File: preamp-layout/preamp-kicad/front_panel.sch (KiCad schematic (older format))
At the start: 0 parts

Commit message: general layout work
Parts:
- added SW? (x6): SW_Push_Open, symbol Switch:SW_Push_Open
- added U?: 4021, symbol 4xxx:4021
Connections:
- net CLK: now also U?.10 (CP)
- net MISO: now also U?.3 (Q7)
- net MOSI: now also U?.11 (DS)
- new net 5V: SW?.1 (A), SW?.1 (A), SW?.1 (A), SW?.1 (A), SW?.1 (A), SW?.1 (A), U?.16 (VDD)
- new net CS: U?.9 (PL)
- new net GNDD: U?.8 (VSS)
- new net SW_CH1: SW?.2 (B), U?.7 (D0)
- new net SW_CH2: SW?.2 (B), U?.6 (D1)
- new net SW_CH3: SW?.2 (B), U?.5 (D2)
- new net SW_CH4: SW?.2 (B), U?.4 (D3)
- new net SW_CH5: SW?.2 (B), U?.13 (D4)
- new net SW_MUTE: SW?.2 (B), U?.14 (D5)
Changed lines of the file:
@@
 $Descr A4 11693 8268
 encoding utf-8
-Sheet 6 11
+Sheet 13 13
 Title ""
 Date ""
@@
 Comment4 ""
 $EndDescr
-Text HLabel 3950 3500 0    50   Output ~ 0
+$Comp
+L Switch:SW_Push_Open SW?
+U 1 1 639B5052
+P 5150 2450
+F 0 "SW?" V 5104 2527 50  0000 L CNN
+F 1 "SW_Push_Open" V 5195 2527 50  0000 L CNN
+F 2 "" H 5150 2650 50  0001 C CNN
+F 3 "~" H 5150 2650 50  0001 C CNN
+	1    5150 2450
+	0    1    1    0
+$EndComp
+Text GLabel 5150 2250 1    50   UnSpc ~ 0
+5V
+$Comp
+L Switch:SW_Push_Open SW?
+U 1 1 639B5BA4
+P 5950 2450
+F 0 "SW?" V 5904 2527 50  0000 L CNN
+F 1 "SW_Push_Open" V 5995 2527 50  0000 L CNN
+F 2 "" H 5950 2650 50  0001 C CNN
+F 3 "~" H 5950 2650 50  0001 C CNN
+	1    5950 2450
+	0    1    1    0
+$EndComp
+Text GLabel 5950 2250 1    50   UnSpc ~ 0
+5V
+$Comp
+L Switch:SW_Push_Open SW?
+U 1 1 639B6392
+P 6750 2450
+F 0 "SW?" V 6704 2527 50  0000 L CNN
+F 1 "SW_Push_Open" V 6795 2527 50  0000 L CNN
+F 2 "" H 6750 2650 50  0001 C CNN
+F 3 "~" H 6750 2650 50  0001 C CNN
+	1    6750 2450
+	0    1    1    0
+$EndComp
+Text GLabel 6750 2250 1    50   UnSpc ~ 0
+5V
+$Comp
+L Switch:SW_Push_Open SW?
+U 1 1 639B63A7
+P 7550 2450
+F 0 "SW?" V 7504 2527 50  0000 L CNN
+F 1 "SW_Push_Open" V 7595 2527 50  0000 L CNN
+F 2 "" H 7550 2650 50  0001 C CNN
+F 3 "~" H 7550 2650 50  0001 C CNN
+	1    7550 2450
+	0    1    1    0
+$EndComp
+Text GLabel 7550 2250 1    50   UnSpc ~ 0
+5V
+$Comp
+L Switch:SW_Push_Open SW?
+U 1 1 639B8372
+P 8350 2450
+F 0 "SW?" V 8304 2527 50  0000 L CNN
+F 1 "SW_Push_Open" V 8395 2527 50  0000 L CNN
+F 2 "" H 8350 2650 50  0001 C CNN
+F 3 "~" H 8350 2650 50  0001 C CNN
+	1    8350 2450
+	0    1    1    0
+$EndComp
+Text GLabel 8350 2250 1    50   UnSpc ~ 0
+5V
+$Comp
+L Switch:SW_Push_Open SW?
+U 1 1 639B8387
+P 9150 2450
+F 0 "SW?" V 9104 2527 50  0000 L CNN
+F 1 "SW_Push_Open" V 9195 2527 50  0000 L CNN
+F 2 "" H 9150 2650 50  0001 C CNN
+F 3 "~" H 9150 2650 50  0001 C CNN
+	1    9150 2450
+	0    1    1    0
+$EndComp
+Text GLabel 9150 2250 1    50   UnSpc ~ 0
+5V
+$Comp
+L 4xxx:4021 U?
+U 1 1 639BBE1A
+P 10100 4550
+F 0 "U?" H 10100 5531 50  0000 C CNN
+F 1 "4021" H 10100 5440 50  0000 C CNN
+F 2 "" H 10100 4700 50  0001 C CNN
+F 3 "https://assets.nexperia.com/documents/data-sheet/HEF4021B.pdf" H 10100 4700 50  0001 C CNN
+	1    10100 4550
+	1    0    0    -1
+$EndComp
+Text GLabel 10100 3450 1    50   UnSpc ~ 0
+5V
+Wire Wire Line
+	10100 3750 10100 3450
+Text Label 9550 4450 2    50   ~ 0
+SW_CH1
+Text Label 9550 4550 2    50   ~ 0
+SW_CH2
+Text Label 9550 4650 2    50   ~ 0
+SW_CH3
+Text Label 9550 4750 2    50   ~ 0
+SW_CH4
+Text Label 9550 4850 2    50   ~ 0
+SW_CH5
+Text Label 9550 4950 2    50   ~ 0
+SW_MUTE
+Wire Wire Line
+	9700 4450 9550 4450
+Wire Wire Line
+	9550 4650 9700 4650
+Wire Wire Line
+	9550 4550 9700 4550
+Wire Wire Line
+	9700 4750 9550 4750
+Wire Wire Line
+	9700 4850 9550 4850
+Wire Wire Line
+	9700 4950 9550 4950
+$Comp
+L power:GNDD #PWR?
+U 1 1 639C488C
+P 10100 5350
+F 0 "#PWR?" H 10100 5100 50  0001 C CNN
+F 1 "GNDD" H 10104 5195 50  0000 C CNN
+F 2 "" H 10100 5350 50  0001 C CNN
+F 3 "" H 10100 5350 50  0001 C CNN
+	1    10100 5350
+	1    0    0    -1
+$EndComp
+Text HLabel 10650 4150 2    50   Output ~ 0
 MISO
-Text HLabel 3950 3700 0    50   Input ~ 0
+Text HLabel 9550 4250 0    50   Input ~ 0
 MOSI
-Text HLabel 3950 3900 0    50   Input ~ 0
+Text HLabel 9550 3950 0    50   Input ~ 0
 CLK
-Text HLabel 3950 4100 0    50   Input ~ 0
-CS_VOL_LIGHT
-Text HLabel 3950 4300 0    50   Input ~ 0
-CS_SELECT_LIGHT
-Text HLabel 3950 4500 0    50   Input ~ 0
-CS_VOL_ENCODER
-Text HLabel 3950 4700 0    50   Input ~ 0
-CS_SELECT_ENCODER
+Text HLabel 9550 4150 0    50   Input ~ 0
+CS
+Wire Wire Line
+	9550 4250 9700 4250
+Wire Wire Line
+	9550 4150 9700 4150
+Wire Wire Line
+	9550 3950 9700 3950
+Wire Wire Line
+	10500 4150 10650 4150
+Text Label 5150 2650 3    50   ~ 0
+SW_CH1
+Text Label 5950 2650 3    50   ~ 0
+SW_CH2
+Text Label 6750 2650 3    50   ~ 0
+SW_CH3
+Text Label 7550 2650 3    50   ~ 0
+SW_CH4
+Text Label 8350 2650 3    50   ~ 0
+SW_CH5
+Text Label 9150 2650 3    50   ~ 0
+SW_MUTE
+Text HLabel 6900 4000 2    50   UnSpc ~ 0
+tone_ctl_1
+Text HLabel 6900 4150 2    50   UnSpc ~ 0
+tone_ctl_2
+Text HLabel 6900 4300 2    50   UnSpc ~ 0
+tone_ctl_3
 $EndSCHEMATC

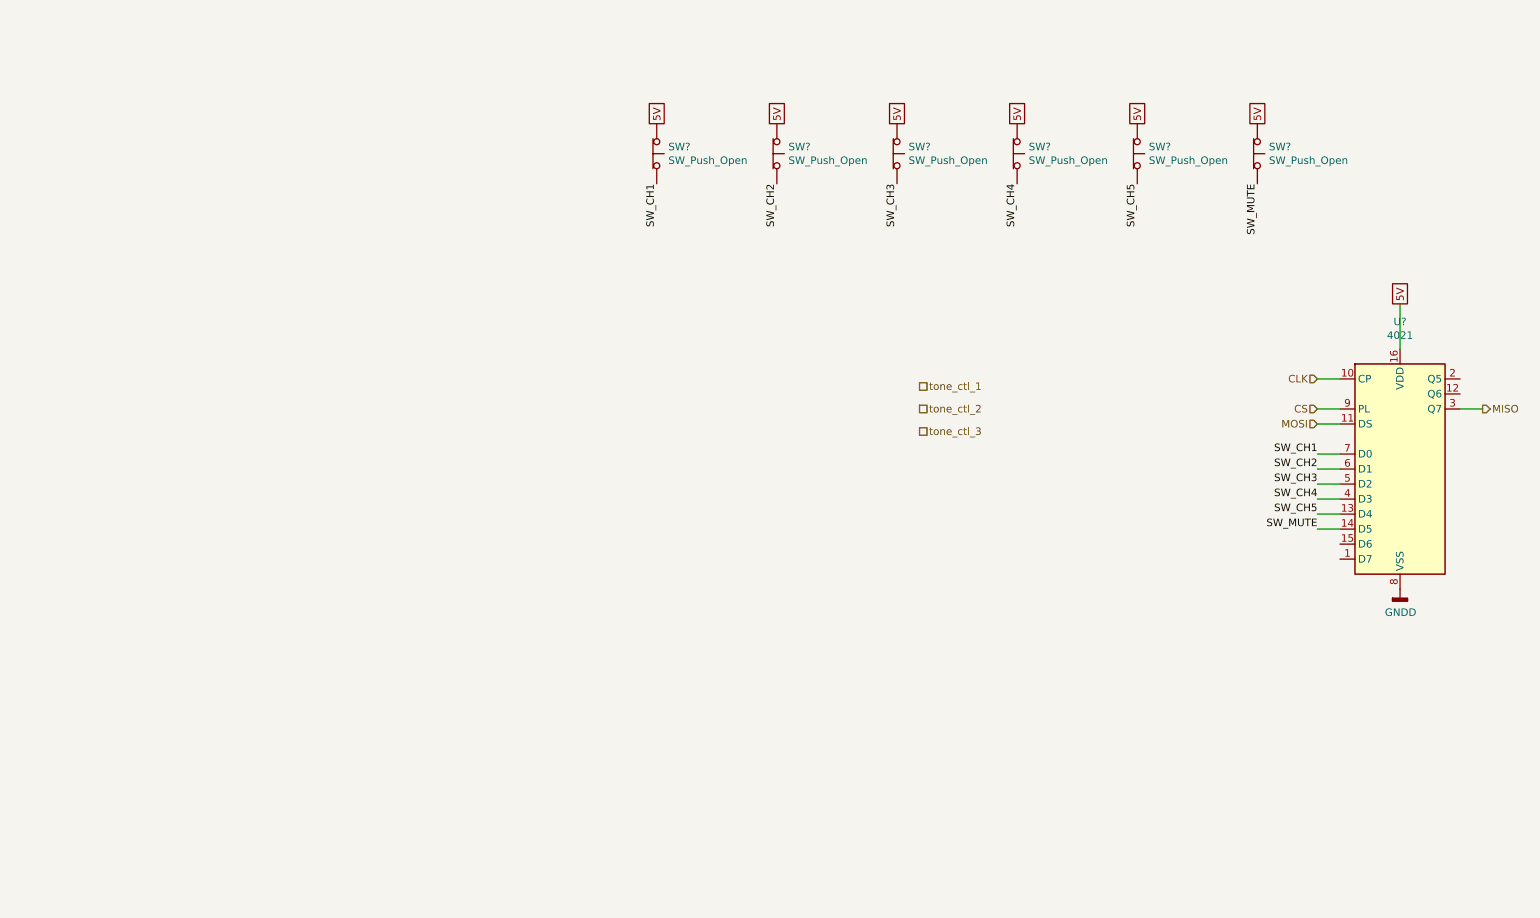
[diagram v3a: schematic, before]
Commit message: Encoder, LED, front panel update
Removed hierarchical sheets for encoders, moved encoders to main sheet. Added switches for output select on front panel sheet. Added LEDs on front panel sheet but only as a symbol, only two instances currently present. Added LED data line between MCU and front panel.
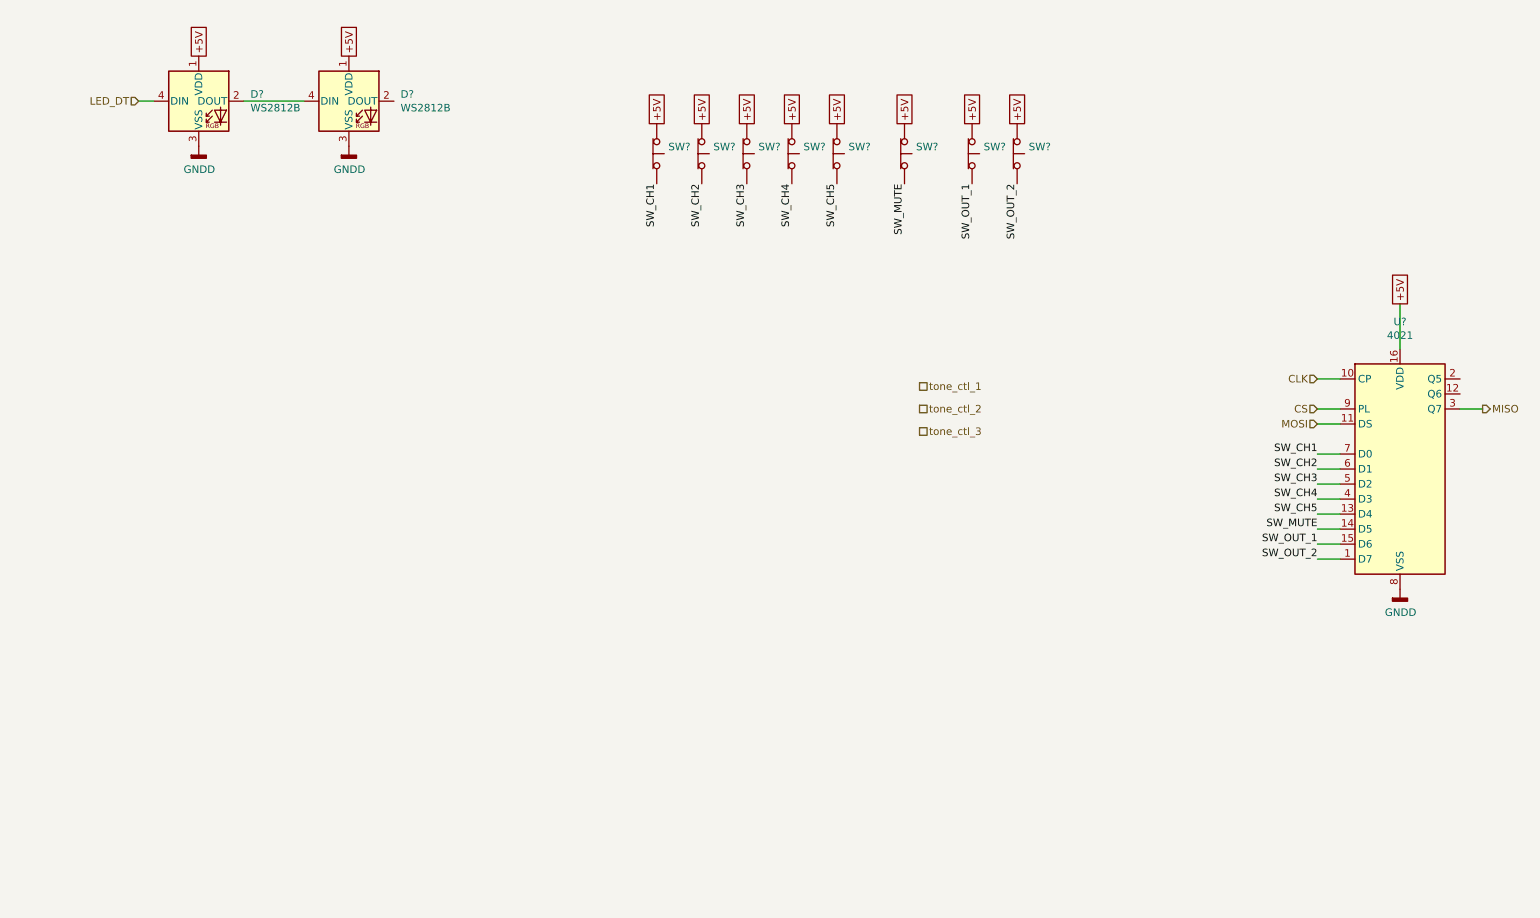
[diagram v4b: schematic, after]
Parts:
- added D? (x2): WS2812B, LED_SMD:LED_WS2812B_PLCC4_5.0x5.0mm_P3.2mm, symbol LED:WS2812B
- added SW? (x2): SW_Push_Open, symbol Switch:SW_Push_Open
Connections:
- net GNDD: now also D?.3 (VSS), D?.3 (VSS)
- net SW_OUT_2: now reaches U?.1 (D7)
- net SW_OUT_2: now also SW?.2 (B)
- net SW_OUT_1: now reaches U?.15 (D6)
- net SW_OUT_1: now also SW?.2 (B)
- net 5V renamed +5V
- net +5V: now also D?.1 (VDD), D?.1 (VDD), SW?.1 (A), SW?.1 (A)
- new net: D?.2 (DOUT), D?.4 (DIN)
- new net LED_DT: D?.4 (DIN)
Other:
- moved on the sheet: SW?
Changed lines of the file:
@@
 $Descr A4 11693 8268
 encoding utf-8
-Sheet 13 14
+Sheet 9 12
 Title ""
 Date ""
@@
 Comment4 ""
 $EndDescr
-$Comp
-L Switch:SW_Push_Open SW?
-U 1 1 639B5052
-P 5150 2450
-F 0 "SW?" V 5104 2527 50  0000 L CNN
-F 1 "SW_Push_Open" V 5195 2527 50  0000 L CNN
-F 2 "" H 5150 2650 50  0001 C CNN
-F 3 "~" H 5150 2650 50  0001 C CNN
-	1    5150 2450
-	0    1    1    0
-$EndComp
 Text GLabel 5150 2250 1    50   UnSpc ~ 0
-5V
++5V
 $Comp
 L Switch:SW_Push_Open SW?
 U 1 1 639B5BA4
-P 5950 2450
-F 0 "SW?" V 5904 2527 50  0000 L CNN
-F 1 "SW_Push_Open" V 5995 2527 50  0000 L CNN
-F 2 "" H 5950 2650 50  0001 C CNN
-F 3 "~" H 5950 2650 50  0001 C CNN
-	1    5950 2450
-	0    1    1    0
-$EndComp
-Text GLabel 5950 2250 1    50   UnSpc ~ 0
-5V
+P 5450 2450
+F 0 "SW?" V 5404 2527 50  0000 L CNN
+F 1 "SW_Push_Open" V 5495 2527 50  0001 L CNN
+F 2 "" H 5450 2650 50  0001 C CNN
+F 3 "~" H 5450 2650 50  0001 C CNN
+	1    5450 2450
+	0    1    1    0
+$EndComp
+Text GLabel 5450 2250 1    50   UnSpc ~ 0
++5V
 $Comp
 L Switch:SW_Push_Open SW?
 U 1 1 639B6392
-P 6750 2450
-F 0 "SW?" V 6704 2527 50  0000 L CNN
-F 1 "SW_Push_Open" V 6795 2527 50  0000 L CNN
-F 2 "" H 6750 2650 50  0001 C CNN
-F 3 "~" H 6750 2650 50  0001 C CNN
-	1    6750 2450
-	0    1    1    0
-$EndComp
-Text GLabel 6750 2250 1    50   UnSpc ~ 0
-5V
+P 5750 2450
+F 0 "SW?" V 5704 2527 50  0000 L CNN
+F 1 "SW_Push_Open" V 5795 2527 50  0001 L CNN
+F 2 "" H 5750 2650 50  0001 C CNN
+F 3 "~" H 5750 2650 50  0001 C CNN
+	1    5750 2450
+	0    1    1    0
+$EndComp
+Text GLabel 5750 2250 1    50   UnSpc ~ 0
++5V
 $Comp
 L Switch:SW_Push_Open SW?
 U 1 1 639B63A7
-P 7550 2450
-F 0 "SW?" V 7504 2527 50  0000 L CNN
-F 1 "SW_Push_Open" V 7595 2527 50  0000 L CNN
-F 2 "" H 7550 2650 50  0001 C CNN
-F 3 "~" H 7550 2650 50  0001 C CNN
-	1    7550 2450
-	0    1    1    0
-$EndComp
-Text GLabel 7550 2250 1    50   UnSpc ~ 0
-5V
+P 6050 2450
+F 0 "SW?" V 6004 2527 50  0000 L CNN
+F 1 "SW_Push_Open" V 6095 2527 50  0001 L CNN
+F 2 "" H 6050 2650 50  0001 C CNN
+F 3 "~" H 6050 2650 50  0001 C CNN
+	1    6050 2450
+	0    1    1    0
+$EndComp
+Text GLabel 6050 2250 1    50   UnSpc ~ 0
++5V
 $Comp
 L Switch:SW_Push_Open SW?
 U 1 1 639B8372
-P 8350 2450
-F 0 "SW?" V 8304 2527 50  0000 L CNN
-F 1 "SW_Push_Open" V 8395 2527 50  0000 L CNN
-F 2 "" H 8350 2650 50  0001 C CNN
-F 3 "~" H 8350 2650 50  0001 C CNN
-	1    8350 2450
-	0    1    1    0
-$EndComp
-Text GLabel 8350 2250 1    50   UnSpc ~ 0
-5V
+P 6350 2450
+F 0 "SW?" V 6304 2527 50  0000 L CNN
+F 1 "SW_Push_Open" V 6395 2527 50  0001 L CNN
+F 2 "" H 6350 2650 50  0001 C CNN
+F 3 "~" H 6350 2650 50  0001 C CNN
+	1    6350 2450
+	0    1    1    0
+$EndComp
+Text GLabel 6350 2250 1    50   UnSpc ~ 0
++5V
 $Comp
 L Switch:SW_Push_Open SW?
 U 1 1 639B8387
-P 9150 2450
-F 0 "SW?" V 9104 2527 50  0000 L CNN
-F 1 "SW_Push_Open" V 9195 2527 50  0000 L CNN
-F 2 "" H 9150 2650 50  0001 C CNN
-F 3 "~" H 9150 2650 50  0001 C CNN
-	1    9150 2450
-	0    1    1    0
-$EndComp
-Text GLabel 9150 2250 1    50   UnSpc ~ 0
-5V
+P 6800 2450
+F 0 "SW?" V 6754 2527 50  0000 L CNN
+F 1 "SW_Push_Open" V 6845 2527 50  0001 L CNN
+F 2 "" H 6800 2650 50  0001 C CNN
+F 3 "~" H 6800 2650 50  0001 C CNN
+	1    6800 2450
+	0    1    1    0
+$EndComp
+Text GLabel 6800 2250 1    50   UnSpc ~ 0
++5V
 $Comp
 L 4xxx:4021 U?
@@
 $EndComp
 Text GLabel 10100 3450 1    50   UnSpc ~ 0
-5V
++5V
 Wire Wire Line
 	10100 3750 10100 3450
@@
 Text Label 5150 2650 3    50   ~ 0
 SW_CH1
-Text Label 5950 2650 3    50   ~ 0
+Text Label 5450 2650 3    50   ~ 0
 SW_CH2
-Text Label 6750 2650 3    50   ~ 0
+Text Label 5750 2650 3    50   ~ 0
 SW_CH3
-Text Label 7550 2650 3    50   ~ 0
+Text Label 6050 2650 3    50   ~ 0
 SW_CH4
-Text Label 8350 2650 3    50   ~ 0
+Text Label 6350 2650 3    50   ~ 0
 SW_CH5
-Text Label 9150 2650 3    50   ~ 0
+Text Label 6800 2650 3    50   ~ 0
 SW_MUTE
 Text HLabel 6900 4000 2    50   UnSpc ~ 0
@@
 Text HLabel 6900 4300 2    50   UnSpc ~ 0
 tone_ctl_3
+$Comp
+L LED:WS2812B D?
+U 1 1 5EA014C6
+P 2100 2100
+F 0 "D?" H 2444 2146 50  0000 L CNN
+F 1 "WS2812B" H 2444 2055 50  0000 L CNN
+F 2 "LED_SMD:LED_WS2812B_PLCC4_5.0x5.0mm_P3.2mm" H 2150 1800 50  0001 L TNN
+F 3 "https://cdn-shop.adafruit.com/datasheets/WS2812B.pdf" H 2200 1725 50  0001 L TNN
+	1    2100 2100
+	1    0    0    -1
+$EndComp
+$Comp
+L Switch:SW_Push_Open SW?
+U 1 1 5EA015B7
+P 7250 2450
+F 0 "SW?" V 7204 2527 50  0000 L CNN
+F 1 "SW_Push_Open" V 7295 2527 50  0001 L CNN
+F 2 "" H 7250 2650 50  0001 C CNN
+F 3 "~" H 7250 2650 50  0001 C CNN
+	1    7250 2450
+	0    1    1    0
+$EndComp
+Text GLabel 7250 2250 1    50   UnSpc ~ 0
++5V
+Text Label 7250 2650 3    50   ~ 0
+SW_OUT_1
+$Comp
+L Switch:SW_Push_Open SW?
+U 1 1 5EA0246D
+P 7550 2450
+F 0 "SW?" V 7504 2527 50  0000 L CNN
+F 1 "SW_Push_Open" V 7595 2527 50  0001 L CNN
+F 2 "" H 7550 2650 50  0001 C CNN
+F 3 "~" H 7550 2650 50  0001 C CNN
+	1    7550 2450
+	0    1    1    0
+$EndComp
+Text GLabel 7550 2250 1    50   UnSpc ~ 0
++5V
+Text Label 7550 2650 3    50   ~ 0
+SW_OUT_2
+Text Label 9550 5050 2    50   ~ 0
+SW_OUT_1
+Text Label 9550 5150 2    50   ~ 0
+SW_OUT_2
+Wire Wire Line
+	9700 5050 9550 5050
+Wire Wire Line
+	9550 5150 9700 5150
+$Comp
+L power:GNDD #PWR?
+U 1 1 5EA03907
+P 2100 2400
+F 0 "#PWR?" H 2100 2150 50  0001 C CNN
+F 1 "GNDD" H 2104 2245 50  0000 C CNN
+F 2 "" H 2100 2400 50  0001 C CNN
+F 3 "" H 2100 2400 50  0001 C CNN
+	1    2100 2400
+	1    0    0    -1
+$EndComp
+Text GLabel 2100 1800 1    50   UnSpc ~ 0
++5V
+$Comp
+L LED:WS2812B D?
+U 1 1 5EA04D89
+P 3100 2100
+F 0 "D?" H 3444 2146 50  0000 L CNN
+F 1 "WS2812B" H 3444 2055 50  0000 L CNN
+F 2 "LED_SMD:LED_WS2812B_PLCC4_5.0x5.0mm_P3.2mm" H 3150 1800 50  0001 L TNN
+F 3 "https://cdn-shop.adafruit.com/datasheets/WS2812B.pdf" H 3200 1725 50  0001 L TNN
+	1    3100 2100
+	1    0    0    -1
+$EndComp
+$Comp
+L power:GNDD #PWR?
+U 1 1 5EA04D93
+P 3100 2400
+F 0 "#PWR?" H 3100 2150 50  0001 C CNN
+F 1 "GNDD" H 3104 2245 50  0000 C CNN
+F 2 "" H 3100 2400 50  0001 C CNN
+F 3 "" H 3100 2400 50  0001 C CNN
+	1    3100 2400
+	1    0    0    -1
+$EndComp
+Text GLabel 3100 1800 1    50   UnSpc ~ 0
++5V
+Wire Wire Line
+	2400 2100 2800 2100
+$Comp
+L Switch:SW_Push_Open SW?
+U 1 1 639B5052
+P 5150 2450
+F 0 "SW?" V 5104 2527 50  0000 L CNN
+F 1 "SW_Push_Open" V 5195 2527 50  0001 L CNN
+F 2 "" H 5150 2650 50  0001 C CNN
+F 3 "~" H 5150 2650 50  0001 C CNN
+	1    5150 2450
+	0    1    1    0
+$EndComp
+Text HLabel 1700 2100 0    50   Input ~ 0
+LED_DT
+Wire Wire Line
+	1700 2100 1800 2100
 $EndSCHEMATC

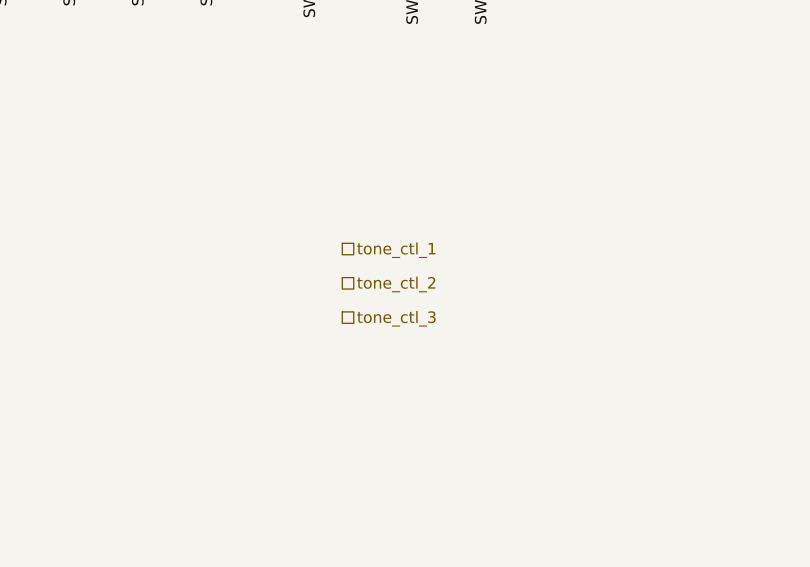
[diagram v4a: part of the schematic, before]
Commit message: Tone Control update
Generated analog tone controls controlled either by pots mounted on the front panel or encoders mounted on the front panel that communicate to the tone control board via SPI.
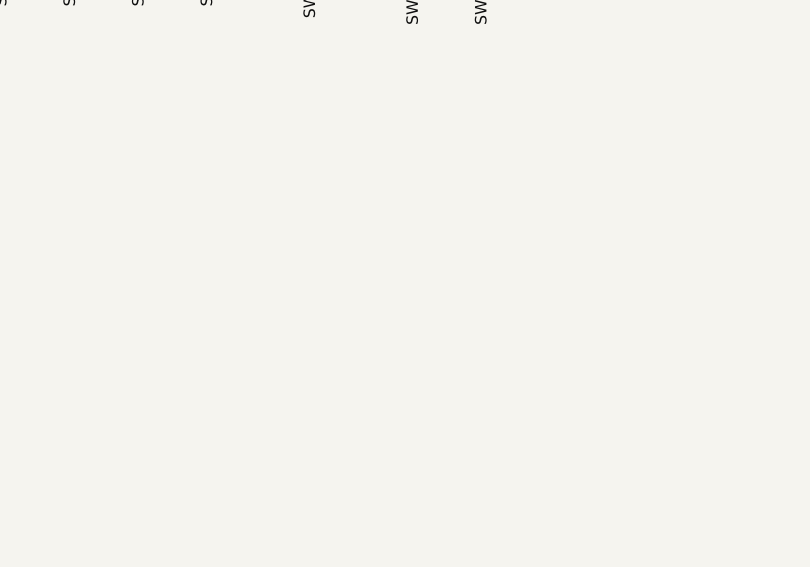
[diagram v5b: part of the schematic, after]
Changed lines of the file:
@@
 $Descr A4 11693 8268
 encoding utf-8
-Sheet 9 12
+Sheet 9 13
 Title ""
 Date ""
@@
 Text Label 6800 2650 3    50   ~ 0
 SW_MUTE
-Text HLabel 6900 4000 2    50   UnSpc ~ 0
-tone_ctl_1
-Text HLabel 6900 4150 2    50   UnSpc ~ 0
-tone_ctl_2
-Text HLabel 6900 4300 2    50   UnSpc ~ 0
-tone_ctl_3
 $Comp
 L LED:WS2812B D?
 U 1 1 5EA014C6
 P 2100 2100
+AR Path="/5EA014C6" Ref="D?"  Part="1"
+AR Path="/5E5ECAAE/5EA014C6" Ref="D?"  Part="1"
 F 0 "D?" H 2444 2146 50  0000 L CNN
 F 1 "WS2812B" H 2444 2055 50  0000 L CNN
@@
 U 1 1 5EA04D89
 P 3100 2100
+AR Path="/5EA04D89" Ref="D?"  Part="1"
+AR Path="/5E5ECAAE/5EA04D89" Ref="D?"  Part="1"
 F 0 "D?" H 3444 2146 50  0000 L CNN
 F 1 "WS2812B" H 3444 2055 50  0000 L CNN
